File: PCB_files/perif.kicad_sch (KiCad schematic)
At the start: 35 parts, among them SW1 SW_Push, SW2 SW_Push, SW3 SW_Push, SW4 SW_Push, SW5 SW_Push, SW6 SW_Push, U7 SN65HVD234, U8 MCP2515-xST, Y1 16Mhz

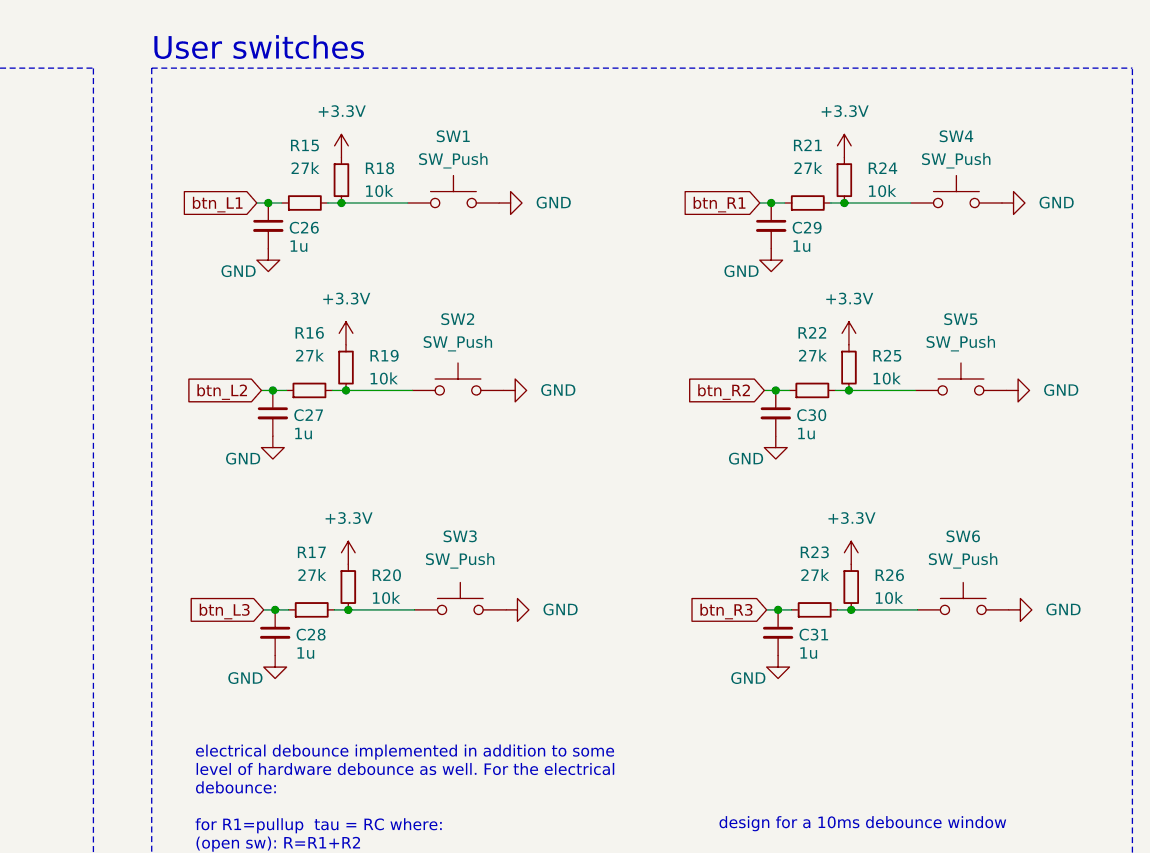
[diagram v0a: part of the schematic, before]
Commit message: r1a upload
uploaded files for r1a; correct button numbering
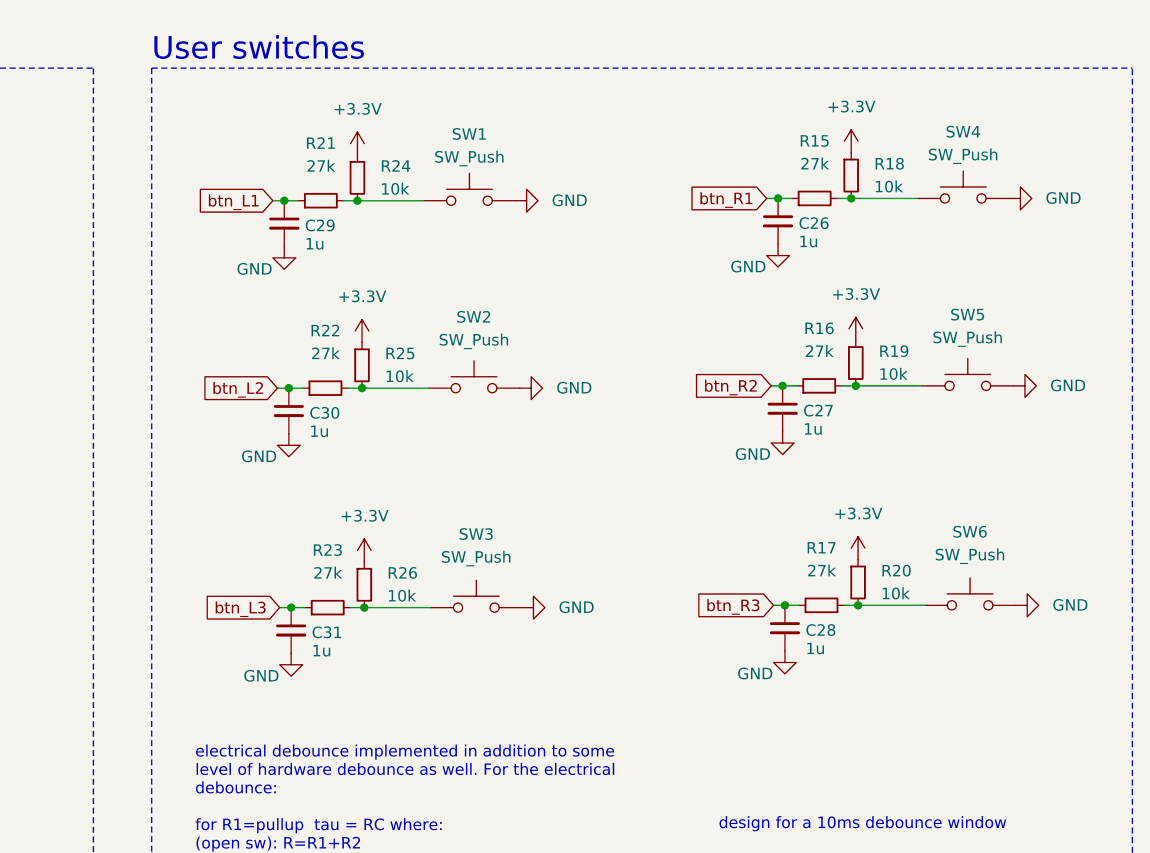
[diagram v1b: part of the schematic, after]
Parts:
- renumbered SW4 to SW1, SW5 to SW2, SW6 to SW3, SW1 to SW4, SW2 to SW5, SW3 to SW6
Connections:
- net btn_L1: now also C29.1, R21.1; no longer C26.1, R15.1
- net btn_L2: now also C30.1, R22.1; no longer C27.1, R16.1
- net btn_L3: now also C31.1, R23.1; no longer C28.1, R17.1
- net btn_R1: now also C26.1, R15.1; no longer C29.1, R21.1
- net btn_R2: now also C27.1, R16.1; no longer C30.1, R22.1
- net btn_R3: now also C28.1, R17.1; no longer C31.1, R23.1
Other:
- moved on the sheet: C26, C27, C28, C29, C30, C31, R15, R16, R17, R18, R19, R20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

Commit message: push from desktop to align files
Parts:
- renumbered C22 to C25, C29 to C27, C27 to C28, C30 to C29, C28 to C30, C23 to C32, C24 to C33, C25 to C34, D8 to D9, R18 to R13, R24 to R14, R21 to R16, R19 to R17, R25 to R18, R16 to R19, R22 to R20, R14 to R21, R20 to R22, R26 to R23, R17 to R24, R23 to R25, R13 to R26, SW4 to SW2, SW1 to SW3, SW5 to SW4, SW2 to SW5, SW3 to SW7, U7 to U9

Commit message: final BOM and tweaking
Tweaked some dimensions after mechanical assembly. Generated BOM and reviewed against reseller inventory
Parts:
- C25, C32: MPN (none) -> C0805C104M5RACTU; Manufacturer (none) -> Kemet; Mouser_PN 80-C0805C104M5R -> (none); Reseller_P/N (none) -> 80-C0805C104M5R; Source/Reseller (none) -> Mouser
- C26, C27, C28, C29, C30, C31: MPN (none) -> C0805C105M3RACTU; Manufacturer (none) -> Kemet; Mouser_PN 80-C0805C105M3R -> (none); Reseller_P/N (none) -> 80-C0805C105M3R; Source/Reseller (none) -> Mouser
- C33, C34: MPN (none) -> C0805C200F5GACTU; Manufacturer (none) -> Kemet; Mouser_PN 80-C0805C200F5G -> (none); Reseller_P/N (none) -> 80-C0805C200F5G; Source/Reseller (none) -> Mouser
- D9: MPN (none) -> NUP2105LT1G; Manufacturer (none) -> OnSemi; Mouser_PN 863-NUP2105LT1G -> (none); Reseller_P/N (none) -> 863-NUP2105LT1G; Source/Reseller (none) -> Mouser
- NT1: Mouser_PN N/A -> (none); Reseller_P/N (none) -> N/A; Source/Reseller (none) -> N/A
- R13, R14, R17, R18, R21, R22, R23: MPN (none) -> CRCW080510K0FKEA; Manufacturer (none) -> Vishay; Mouser_PN 71-CRCW0805-10K-E3 -> (none); Reseller_P/N (none) -> 71-CRCW0805-10K-E3; Source/Reseller (none) -> Mouser
- R15, R16, R19, R20, R24, R25: MPN (none) -> CRCW080527K0FKEA; Manufacturer (none) -> Vishay; Mouser_PN 71-CRCW0805-27K-E3 -> (none); Reseller_P/N (none) -> 71-CRCW0805-27K-E3; Source/Reseller (none) -> Mouser
- R26: MPN (none) -> CRCW08054K70FKEA; Manufacturer (none) -> Vishay; Mouser_PN 71-CRCW0805-4.7K-E3 -> (none); Reseller_P/N (none) -> 71-CRCW0805-4.7K-E3; Source/Reseller (none) -> Mouser
- SW2, SW3, SW4, SW5, SW6, SW7: MPN (none) -> B3F-5050; Manufacturer (none) -> Omron; Mouser_PN 653-B3F-5050 -> (none); Reseller_P/N (none) -> 653-B3F-5050; Source/Reseller (none) -> Mouser
- U8: MPN (none) -> MCP2515T-E/ST; Manufacturer (none) -> Microchip; Mouser_PN 579-MCP2515T-E/ST -> (none); Reseller_P/N (none) -> 579-MCP2515T-E/ST; Source/Reseller (none) -> Mouser
- U9: MPN (none) -> SN65HVD234DR; Manufacturer (none) -> TI; Mouser_PN 595-SN65HVD234DR -> (none); Reseller_P/N (none) -> 595-SN65HVD234DR; Source/Reseller (none) -> Mouser
- Y1: MPN (none) -> FA-238 16.0000MB-C3; Manufacturer (none) -> Epson; Mouser_PN 732-FA-23816B-C3 -> (none); Reseller_P/N (none) -> 732-FA-23816B-C3; Source/Reseller (none) -> Mouser
